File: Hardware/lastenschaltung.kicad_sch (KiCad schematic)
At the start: 0 parts

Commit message: added voltage regulator to Lastenschaltung
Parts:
- added 100CuF, 22CuF, C? (x2): C, symbol Device:C
- added 2L2uH?: L, symbol Device:L
- added R? (x3): R, symbol Device:R
- added U?: INA180A3, Package_TO_SOT_SMD:SOT-23-5, symbol Amplifier_Current:INA180A3
- added VoltageRegulator?: TPS62163DSGR, Package_SON:WSON-8-1EP_2x2mm_P0.5mm_EP0.9x1.6mm_ThermalVias, symbol Custom_Lib:TPS62163DSGR
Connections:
- new net: R?.1, VoltageRegulator?.8 (PG)
- new net: 2L2uH?.1, VoltageRegulator?.7 (SW)
- new net: R?.1, R?.1, VoltageRegulator?.5 (FB)
- new net +12V: 100CuF.1, 22CuF.1, VoltageRegulator?.2 (VIN), VoltageRegulator?.3 (EN)
- new net +5V_Out: 2L2uH?.2, C?.1, C?.1, R?.2, R?.2, VoltageRegulator?.6 (VOS)
- new net GND: 100CuF.2, 22CuF.2, C?.2, C?.2, R?.2, VoltageRegulator?.1 (PGND), VoltageRegulator?.4 (AGND)
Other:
- note added: "Loadcircuit"
- note added: "Spannungsregler zur Versorgung mit +5V"
- note added: "Spannungsversorgung"

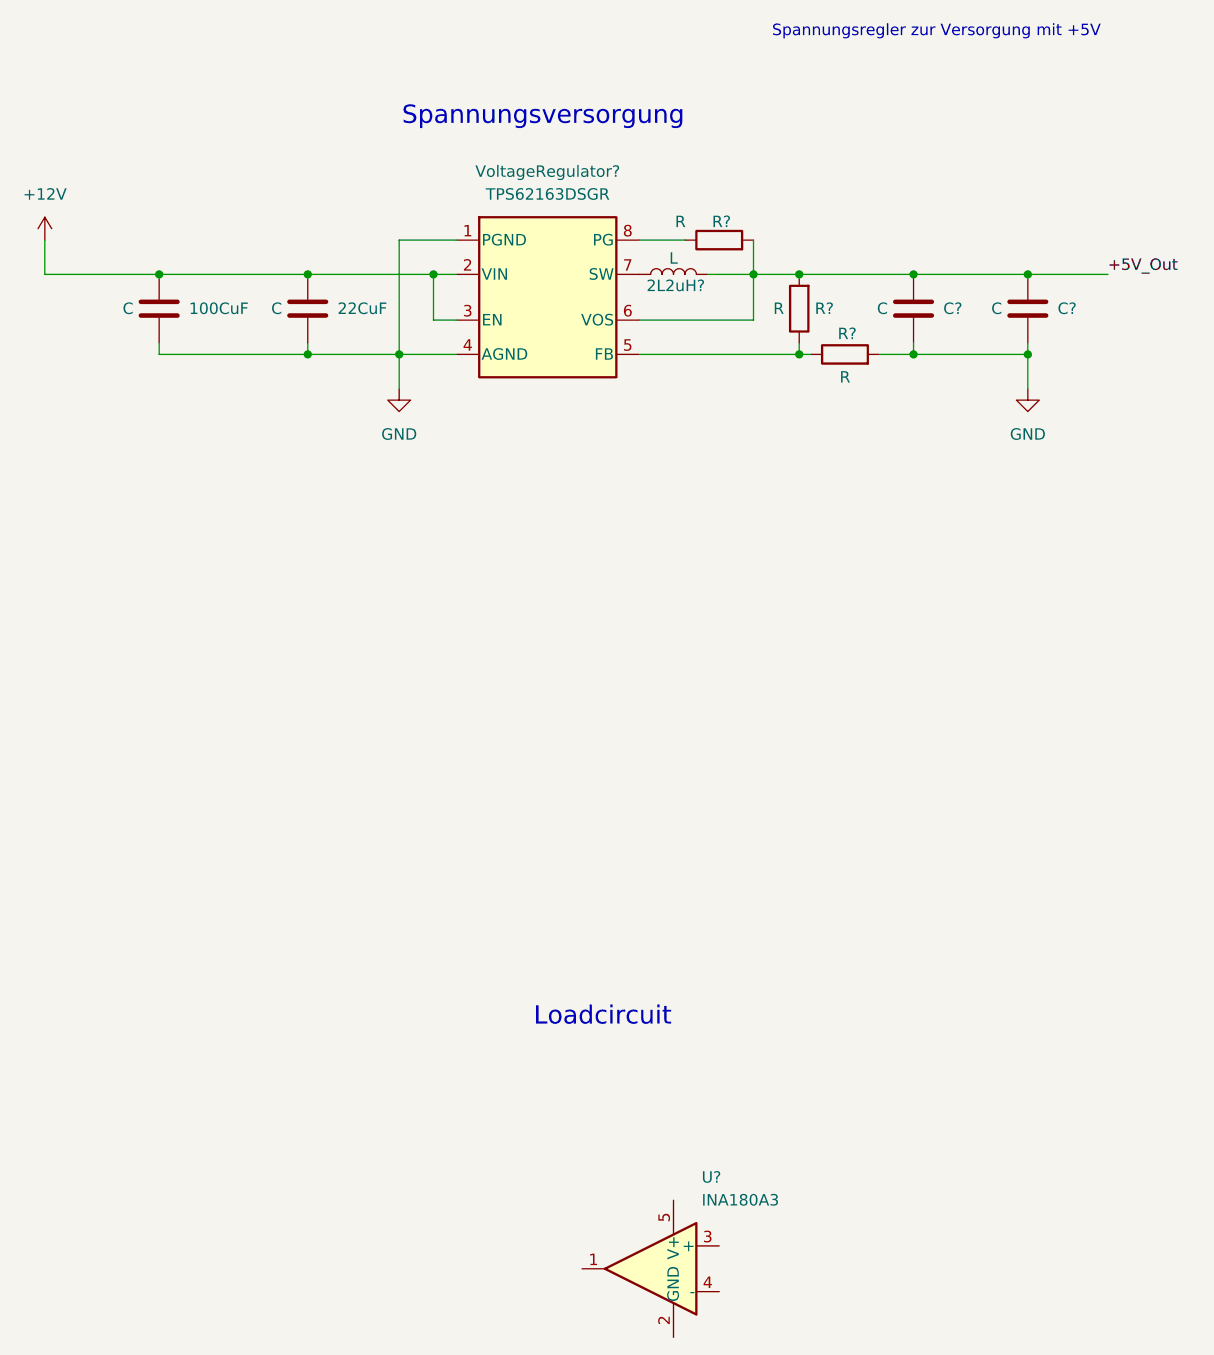
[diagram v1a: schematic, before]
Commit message: added Calculatios for RC-Filter
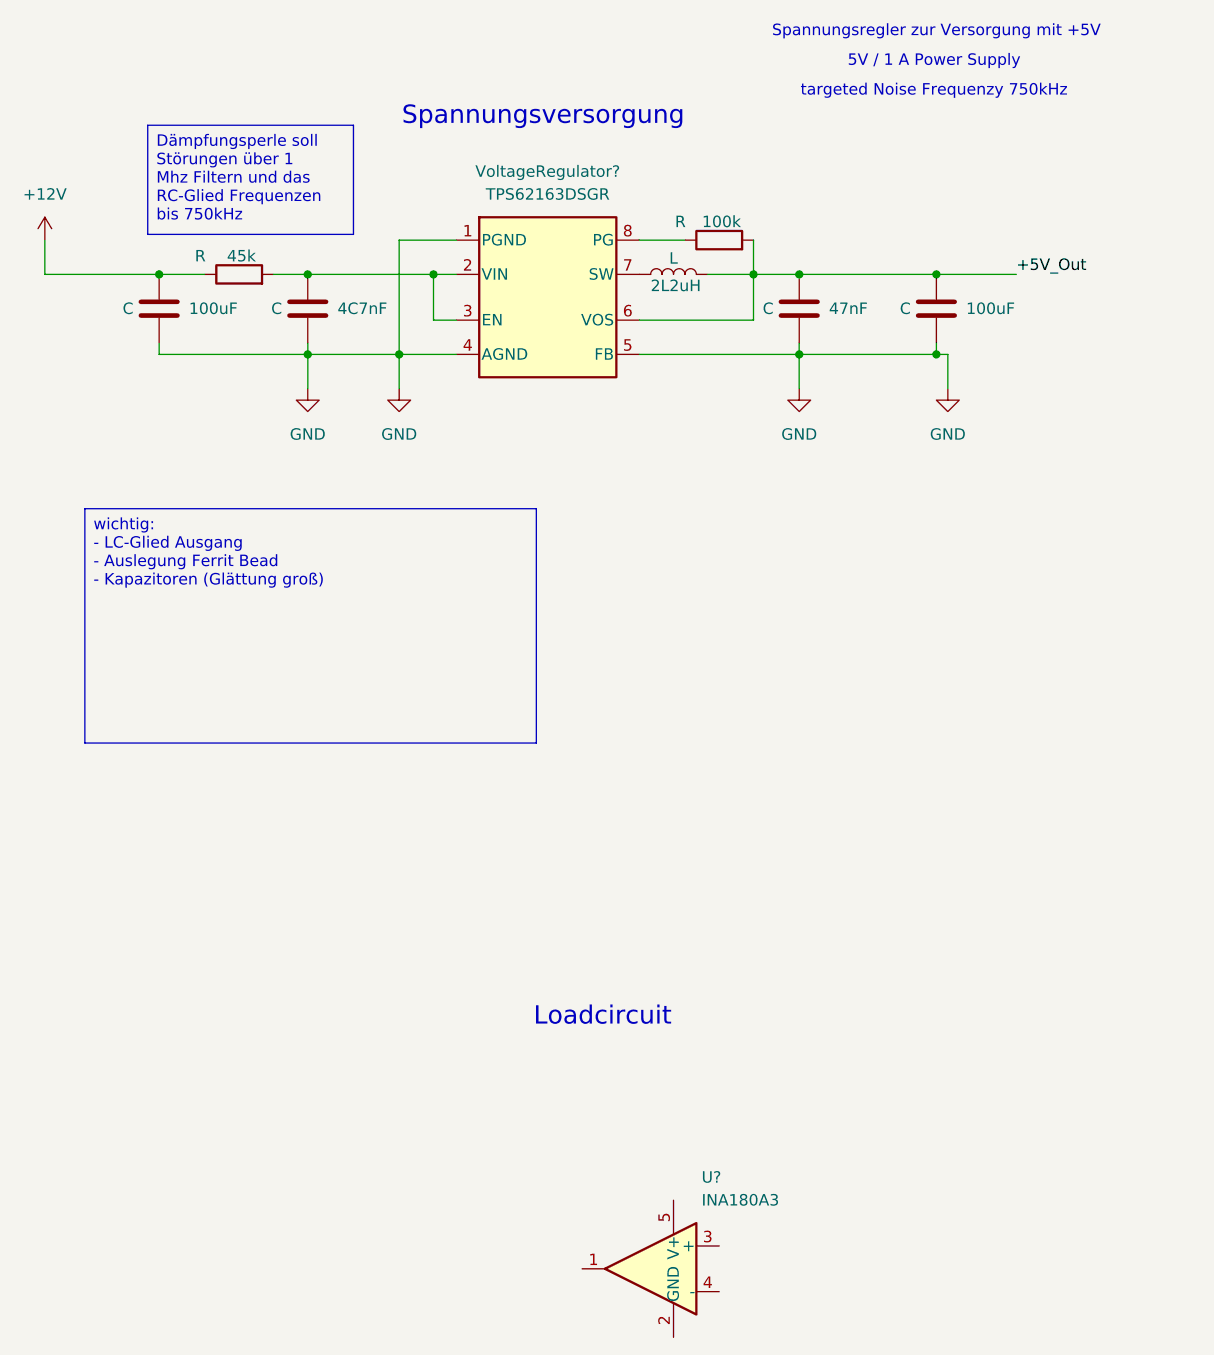
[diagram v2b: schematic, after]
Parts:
- removed R? (x2): R, symbol Device:R
- added 45k: R, symbol Device:R
- gave numbers to parts that had none: 4
- renumbered 100CuF to 100uF, 22CuF to 4C7nF
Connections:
- net +12V: now also 45k.1; no longer 4C7nF.1, VoltageRegulator?.2 (VIN), VoltageRegulator?.3 (EN)
- net GND: now also VoltageRegulator?.5 (FB)
- new net: 45k.2, 4C7nF.1, VoltageRegulator?.2 (VIN), VoltageRegulator?.3 (EN)
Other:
- note added: "5V / 1 A Power Supply"
- note added: "targeted Noise Frequenzy 750kHz"
- moved on the sheet: 100uF, 47nF

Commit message: added additional sources
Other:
- note added: "Frequenzy VR: 2.25MHz"
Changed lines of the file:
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@@
 	(text "targeted Noise Frequenzy 750kHz"
 		(exclude_from_sim no)
-		(at 122.936 27.94 0)
+		(at 119.634 28.448 0)
 		(effects
 			(font
@@
 	(text "5V / 1 A Power Supply\n"
 		(exclude_from_sim no)
-		(at 122.936 24.638 0)
+		(at 114.554 24.892 0)
+		(effects
+			(font
+				(size 1.27 1.27)
+			)
+		)
+	)
+	(text "Frequenzy VR: 2.25MHz"
+		(exclude_from_sim no)
+		(at 114.554 32.004 0)
 		(effects
 			(font
@@
 		)
 	)
-	(text_box "wichtig:\n- LC-Glied Ausgang\n- Auslegung Ferrit Bead\n- Kapazitoren (Glättung groß)"
+	(text_box "wichtig:\n- LC-Glied Ausgang\n- Auslegung Ferrit Bead\n- Kapazitoren (Glättung groß)\n- Widerstand der FB bei 1MHz"
 		(exclude_from_sim no)
 		(at 28.575 74.295 0)
@@
 		)
 	)
+	(text_box "Ferrite Bead Auslegung:\n- 20% über Bias Current\n- DC-Bias bechten\n- I durch R 45K =260uA\n--> 20% Aufschlag +54uA (314uA)\n- FB Verstärkung nicht bei 2.25MHz"
+		(exclude_from_sim no)
+		(at 94.615 74.295 0)
+		(size 45.085 26.035)
+		(margins 0.9525 0.9525 0.9525 0.9525)
+		(stroke
+			(width 0)
+			(type solid)
+		)
+		(fill
+			(type none)
+		)
+		(effects
+			(font
+				(size 1.27 1.27)
+			)
+			(justify left top)
+		)
+	)
 	(text_box "Dämpfungsperle soll Störungen über 1 Mhz Filtern und das RC-Glied Frequenzen bis 750kHz"
 		(exclude_from_sim no)
-		(at 35.56 31.6882 0)
+		(at 38.735 31.6882 0)
 		(size 22.86 12.1268)
 		(margins 0.9525 0.9525 0.9525 0.9525)
@@
 				)
 			)
+			(project "lastenschaltung"
+				(path "/6ce55f68-1125-4cc6-9aee-4afeea746562"
+					(reference "U?")
+					(unit 1)
+				)
+			)
 		)
 	)
@@
 				)
 			)
+			(project "lastenschaltung"
+				(path "/6ce55f68-1125-4cc6-9aee-4afeea746562"
+					(reference "#PWR019")
+					(unit 1)
+				)
+			)
 		)
 	)
@@
 			(project "Prüfschaltung"
 				(path "/50eeda5a-bbbc-4ac4-9402-6cded37e420b"
+					(reference "100k")
+					(unit 1)
+				)
+			)
+			(project "lastenschaltung"
+				(path "/6ce55f68-1125-4cc6-9aee-4afeea746562"
 					(reference "100k")
 					(unit 1)
@@
 				)
 			)
+			(project "lastenschaltung"
+				(path "/6ce55f68-1125-4cc6-9aee-4afeea746562"
+					(reference "#PWR020")
+					(unit 1)
+				)
+			)
 		)
 	)
@@
 				)
 			)
+			(project "lastenschaltung"
+				(path "/6ce55f68-1125-4cc6-9aee-4afeea746562"
+					(reference "#PWR02")
+					(unit 1)
+				)
+			)
 		)
 	)
@@
 				)
 			)
+			(project "lastenschaltung"
+				(path "/6ce55f68-1125-4cc6-9aee-4afeea746562"
+					(reference "100uF")
+					(unit 1)
+				)
+			)
 		)
 	)
@@
 			(project "Prüfschaltung"
 				(path "/50eeda5a-bbbc-4ac4-9402-6cded37e420b"
+					(reference "2L2uH")
+					(unit 1)
+				)
+			)
+			(project "lastenschaltung"
+				(path "/6ce55f68-1125-4cc6-9aee-4afeea746562"
 					(reference "2L2uH")
 					(unit 1)
@@
 				)
 			)
+			(project "lastenschaltung"
+				(path "/6ce55f68-1125-4cc6-9aee-4afeea746562"
+					(reference "VoltageRegulator?")
+					(unit 1)
+				)
+			)
 		)
 	)
@@
 				)
 			)
+			(project "lastenschaltung"
+				(path "/6ce55f68-1125-4cc6-9aee-4afeea746562"
+					(reference "4C7nF")
+					(unit 1)
+				)
+			)
 		)
 	)
@@
 			(project "Prüfschaltung"
 				(path "/50eeda5a-bbbc-4ac4-9402-6cded37e420b"
+					(reference "47nF")
+					(unit 1)
+				)
+			)
+			(project "lastenschaltung"
+				(path "/6ce55f68-1125-4cc6-9aee-4afeea746562"
 					(reference "47nF")
 					(unit 1)
@@
 				)
 			)
+			(project "lastenschaltung"
+				(path "/6ce55f68-1125-4cc6-9aee-4afeea746562"
+					(reference "#PWR021")
+					(unit 1)
+				)
+			)
 		)
 	)
@@
 			(project "Prüfschaltung"
 				(path "/50eeda5a-bbbc-4ac4-9402-6cded37e420b"
+					(reference "45k")
+					(unit 1)
+				)
+			)
+			(project "lastenschaltung"
+				(path "/6ce55f68-1125-4cc6-9aee-4afeea746562"
 					(reference "45k")
 					(unit 1)
@@
 				)
 			)
+			(project "lastenschaltung"
+				(path "/6ce55f68-1125-4cc6-9aee-4afeea746562"
+					(reference "#PWR01")
+					(unit 1)
+				)
+			)
 		)
 	)
@@
 					(reference "100uF")
 					(unit 1)
+				)
+			)
+			(project "lastenschaltung"
+				(path "/6ce55f68-1125-4cc6-9aee-4afeea746562"
+					(reference "100uF")
+					(unit 1)
